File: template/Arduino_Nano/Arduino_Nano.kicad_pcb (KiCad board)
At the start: 2 copper layers, 17.8 x 43.2 mm, 6 parts, among them P1 Digital, P2 Analog, P3 CONN_01X01, P4 CONN_01X01, P5 CONN_01X01, P6 CONN_01X01

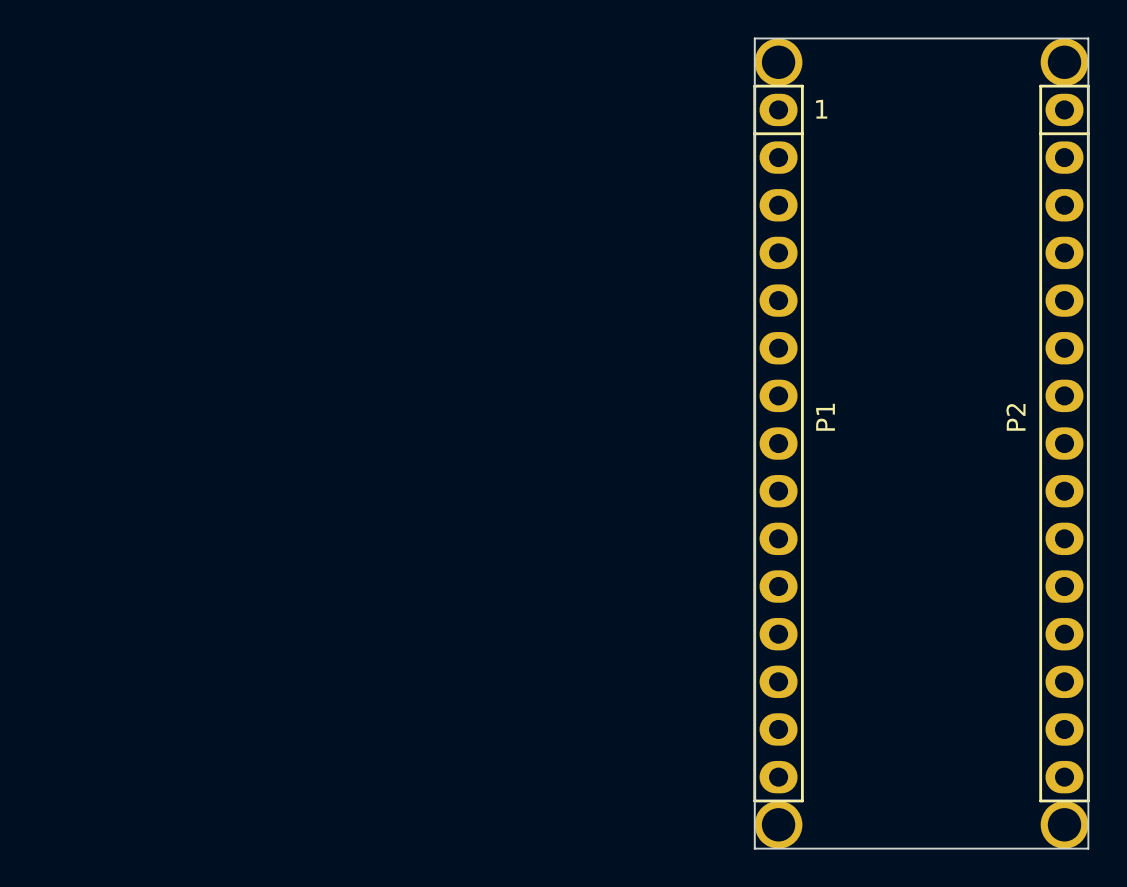
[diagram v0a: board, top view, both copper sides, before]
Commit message: fix: change original libs; add: new components
- Fix LIS3DH pins positions;
- Add ATmega164P symbol;
- Add 3D model to the L_Wuerth_HCM-7050;
- Add parameters for R_RES (Assembly...).
- Add parameters for R_RES and C_CAP;
- Fix SOIC-8 package 3D model;
- Add new parameters for many symbols;
- Change text height from 70 mil to 50 mil;
- Add solder mask expansion for 2-contact jumpers;
- Change thermopad vias of QFN-20-1EP_3x3mm_P0.45mm_EP1.6x1.6mm_ThermalVias;
- Add D_SMAF footprint;
- Fillet silk for C_1206;
-Rectangle silk for R_1206;
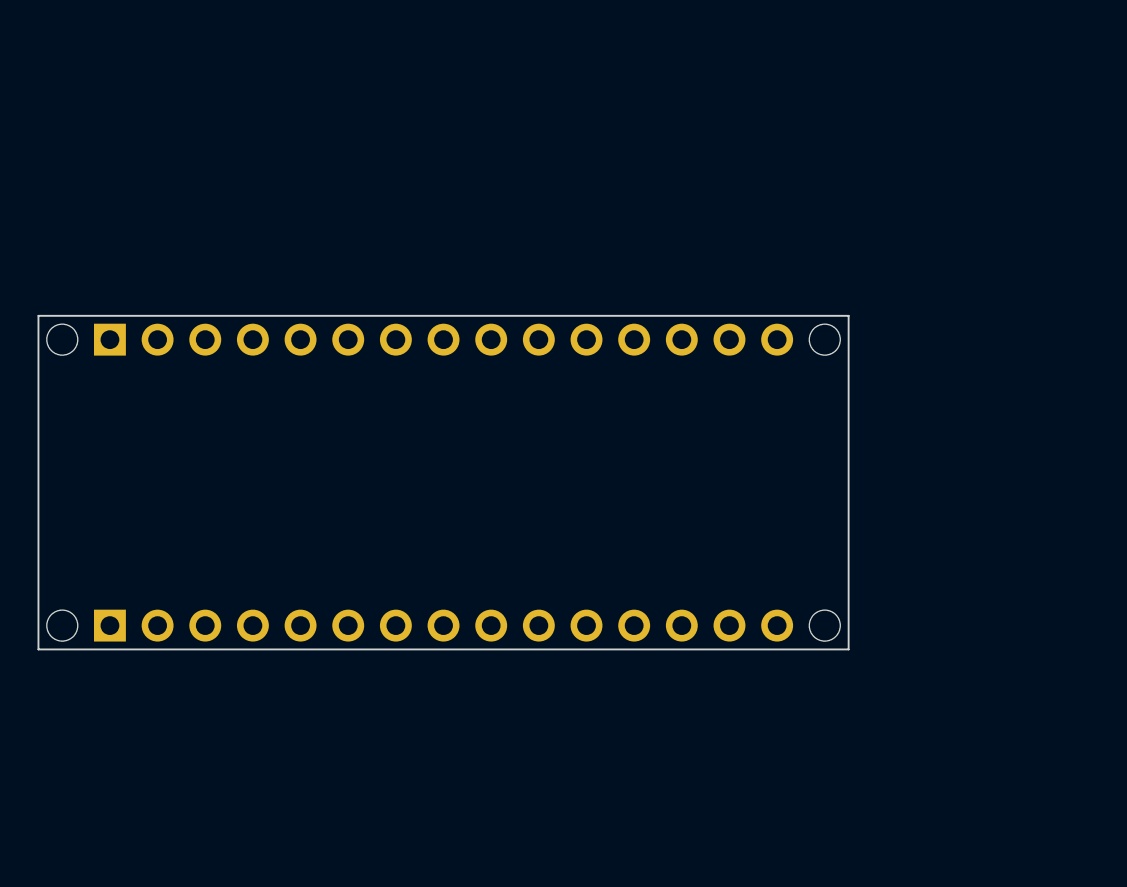
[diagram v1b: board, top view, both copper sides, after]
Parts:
- removed P1: Digital, Socket_Arduino_Nano:Socket_Strip_Arduino_1x15
- removed P2: Analog, Socket_Arduino_Nano:Socket_Strip_Arduino_1x15
- removed P3, P4, P5, P6: CONN_01X01, Socket_Arduino_Nano:1pin_Nano
- added J1: Analog, Connector_PinHeader_2.54mm:PinHeader_1x15_P2.54mm_Vertical, B.Cu at (103.8, 98.7)
- added J2: Digital, Connector_PinHeader_2.54mm:PinHeader_1x15_P2.54mm_Vertical, B.Cu at (103.8, 83.5)
- added MH1: MountingHole_65mil, Arduino_MountingHole:MountingHole_65mil, F.Cu at (101.3, 98.7)
- added MH2: MountingHole_65mil, Arduino_MountingHole:MountingHole_65mil, F.Cu at (101.3, 83.5)
- added MH3: MountingHole_65mil, Arduino_MountingHole:MountingHole_65mil, F.Cu at (141.9, 83.5)
- added MH4: MountingHole_65mil, Arduino_MountingHole:MountingHole_65mil, F.Cu at (141.9, 98.7)
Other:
- board size 17.8 x 43.2 mm -> 43.2 x 17.8 mm
- board text added: "ICSP"
- board text added: "USB Mini-B"
- board text removed: "1"
